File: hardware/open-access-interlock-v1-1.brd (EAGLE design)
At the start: 78.7 x 88.9 mm, 23 parts, among them T1 TIP31

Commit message: Ripping up terminal blocks
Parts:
- removed RELAY: (no value), SparkFun-Connectors:SCREWTERMINAL-3.5MM-3
- added JP1: (no value), SparkFun-Connectors:SCREWTERMINAL-3.5MM-4
- ARDUINO: value ARDUINO_SHIELDNO_SILK -> (none)
- R4: value 650ohm -> 650
- moved T1 44.4 mm to (22.9, 17.8), turned to 180 degrees
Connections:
- removed net N$13: RELAY.2, T1.2
- removed net N$23: ARDUINO.A4, R6.P$1
- removed net N$24: ARDUINO.A5, R7.P$1
- new net RELAY_SIGNAL: JP1.1, T1.2
- net N$14: now also ARDUINO.A4
- net N$15: now also ARDUINO.A5
- net V+: now also JP1.2, JP1.3; no longer RELAY.1
- net V-: now also JP1.4
- net VCC: now also R6.P$1, R7.P$1
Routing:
- net N$23: track 31.1 -> 0.00 mm
- net VCC: track 214.7 -> 189.1 mm
- net RELAY_SIGNAL: track 0.00 -> 23.9 mm
- net N$13: track 15.2 -> 0.00 mm
- net N$14: track 6.61 -> 0.00 mm
- net N$24: track 5.61 -> 0.00 mm
- net N$21: track 8.15 -> 13.5 mm
- net N$15: track 4.48 -> 0.00 mm
- net V-: track 0.00 -> 4.02 mm
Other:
- board text added: "0-24V"
- board text added: "V+"
- board text added: "V-"
- board text removed: "COIL"
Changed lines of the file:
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@@
 <setting verticaltext="up"/>
 </settings>
-<grid distance="50" unitdist="mil" unit="mil" style="dots" multiple="1" display="yes" altdistance="1" altunitdist="mm" altunit="mm"/>
+<grid distance="100" unitdist="mil" unit="mil" style="dots" multiple="1" display="yes" altdistance="1" altunitdist="mm" altunit="mm"/>
 <layers>
 <layer number="1" name="Top" color="4" fill="1" visible="yes" active="yes"/>
@@
 <text x="36.83" y="45.72" size="1.016" layer="25" rot="R90" align="top-left">15</text>
 <text x="36.83" y="48.26" size="1.016" layer="25" rot="R90" align="top-left">16</text>
-<text x="8.89" y="10.16" size="1.016" layer="25" rot="R90" align="top-center">GND</text>
-<text x="8.89" y="13.97" size="1.016" layer="25" rot="R90" align="top-center">COIL</text>
-<text x="8.89" y="17.78" size="1.016" layer="25" rot="R90" align="top-center">+5V</text>
+<text x="8.89" y="21.59" size="1.016" layer="25" align="center-left">GND</text>
+<text x="8.89" y="13.97" size="1.016" layer="25" align="center-left">V-</text>
+<text x="8.89" y="17.78" size="1.016" layer="25" align="center-left">V+</text>
 <text x="8.89" y="69.85" size="1.016" layer="25" rot="R90" align="top-center">+5V</text>
 <text x="8.89" y="66.04" size="1.016" layer="25" rot="R90" align="top-center">GND</text>
@@
 <text x="46.99" y="73.66" size="1.016" layer="25" align="center-right">9</text>
 <text x="46.99" y="55.88" size="1.016" layer="25" align="center">16</text>
+<text x="8.89" y="24.765" size="1.016" layer="25" align="center-left">0-24V</text>
 </plain>
 <attributes>
@@
 </autorouter>
 <elements>
-<element name="ARDUINO" library="SparkFun" package="DUEMILANOVE_VIAS" value="ARDUINO_SHIELDNO_SILK" x="11.43" y="25.4"/>
+<element name="ARDUINO" library="SparkFun" package="DUEMILANOVE_VIAS" value="" x="11.43" y="25.4"/>
 <element name="RELAY_LED" library="led" package="LED5MM" value="GRN" x="73.66" y="12.7" smashed="yes" rot="R90">
 <attribute name="NAME" x="71.8566" y="-0.635" size="1.27" layer="25" ratio="10" rot="R90"/>
@@
 <element name="LCD" library="adafruit" package="LCD1602" value="HD44780LCD-1602" x="68.58" y="2.54" smashed="yes" rot="R90"/>
 <element name="SPKR" library="adafruit" package="PS12" value="SPEAKER/PS12" x="6.35" y="48.26" rot="R180"/>
-<element name="R4" library="SparkFun" package="AXIAL-0.3" value="650ohm" x="24.13" y="35.56" smashed="yes" rot="R180">
+<element name="R4" library="SparkFun" package="AXIAL-0.3" value="650" x="24.13" y="35.56" smashed="yes" rot="R180">
 <attribute name="NAME" x="26.67" y="34.29" size="0.8128" layer="25" font="vector" rot="R180"/>
 <attribute name="VALUE" x="26.162" y="35.941" size="1.016" layer="21" font="vector" ratio="15" rot="R180"/>
@@
 <attribute name="VALUE" x="66.929" y="64.262" size="1.016" layer="21" font="vector" ratio="15" rot="R270"/>
 </element>
-<element name="RELAY" library="SparkFun-Connectors" package="SCREWTERMINAL-3.5MM-3" value="" x="5.08" y="17.78" smashed="yes" rot="R270">
-<attribute name="NAME" x="8.89" y="21.59" size="1.016" layer="25" rot="R180"/>
-<attribute name="VALUE" x="6.35" y="19.05" size="0.4064" layer="27" rot="R270"/>
-</element>
 <element name="READER" library="SparkFun-Connectors" package="SCREWTERMINAL-3.5MM-4" value="" x="5.08" y="69.85" smashed="yes" rot="R270">
 <attribute name="NAME" x="5.08" y="72.39" size="1.016" layer="25"/>
 <attribute name="VALUE" x="6.35" y="71.12" size="0.4064" layer="27" rot="R270"/>
 </element>
-<element name="T1" library="transistor" package="TO220" value="TIP31" x="-17.78" y="0"/>
+<element name="T1" library="transistor" package="TO220" value="TIP31" x="22.86" y="17.78" rot="R180"/>
+<element name="JP1" library="SparkFun-Connectors" package="SCREWTERMINAL-3.5MM-4" value="" x="-5.08" y="-12.7"/>
 </elements>
 <signals>
@@
 <wire x1="13.97" y1="82.55" x2="5.08" y2="73.66" width="0.4064" layer="1"/>
 <contactref element="READER" pad="1"/>
-<wire x1="35.12" y1="13.08" x2="16.13" y2="13.08" width="0.4064" layer="16"/>
-<wire x1="16.13" y1="13.08" x2="11.43" y2="17.78" width="0.4064" layer="16"/>
 <wire x1="5.08" y1="73.66" x2="5.08" y2="69.85" width="0.4064" layer="1"/>
 <wire x1="20.685" y1="74.66" x2="20.685" y2="74.025" width="0.4064" layer="1"/>
@@
 <wire x1="10.16" y1="71.12" x2="8.89" y2="69.85" width="0.4064" layer="1"/>
 <wire x1="8.89" y1="69.85" x2="5.08" y2="69.85" width="0.4064" layer="1"/>
+<contactref element="R6" pad="P$1"/>
+<contactref element="R7" pad="P$1"/>
+<wire x1="48.26" y1="68.58" x2="67.31" y2="66.04" width="0" layer="19" extent="1-1"/>
+<wire x1="71.12" y1="38.1" x2="62.23" y2="41.91" width="0" layer="19" extent="1-1"/>
 </signal>
 <signal name="N$5">
@@
 <contactref element="SHIFT" pad="13"/>
 <contactref element="EXTEND" pad="2"/>
-<contactref element="LOGOUT" pad="2"/>
 <contactref element="ARDUINO" pad="GND@0"/>
-<contactref element="R3" pad="P$1"/>
 <contactref element="SPKR" pad="P$2"/>
 <contactref element="R2" pad="P$1"/>
@@
 <contactref element="READER" pad="2"/>
 <contactref element="R5" pad="P$2"/>
+<contactref element="LOGOUT" pad="2"/>
+<contactref element="R3" pad="P$1"/>
 </signal>
 <signal name="N$3">
@@
 <via x="53.34" y="45.72" extent="1-16" drill="0.3048"/>
 </signal>
-<signal name="N$13">
-<contactref element="RELAY" pad="2"/>
-<wire x1="19.05" y1="16.51" x2="16.51" y2="13.97" width="0.4064" layer="1"/>
-<wire x1="16.51" y1="13.97" x2="5.39" y2="13.97" width="0.4064" layer="1"/>
-<wire x1="5.39" y1="13.97" x2="5.08" y2="14.28" width="0.4064" layer="1"/>
-<contactref element="T1" pad="2"/>
-<wire x1="5.08" y1="14.28" x2="-17.78" y2="-6.35" width="0" layer="19" extent="1-1"/>
-</signal>
 <signal name="N$16">
 <contactref element="RELAY_LED" pad="K"/>
@@
 <contactref element="R5" pad="P$1"/>
 <wire x1="20.32" y1="35.56" x2="20.32" y2="30.48" width="0.4064" layer="1"/>
-<wire x1="20.32" y1="30.48" x2="20.32" y2="29.21" width="0.4064" layer="1"/>
-<wire x1="20.32" y1="29.21" x2="21.59" y2="27.94" width="0.4064" layer="1"/>
 <contactref element="T1" pad="1"/>
-<wire x1="-20.32" y1="-6.35" x2="20.32" y2="29.21" width="0" layer="19" extent="1-1"/>
-</signal>
-<signal name="N$14">
-<contactref element="LOGOUT" pad="4"/>
-<contactref element="R6" pad="P$2"/>
-<wire x1="75.9206" y1="26.1112" x2="75.4888" y2="26.1112" width="0.4064" layer="1"/>
-<wire x1="75.4888" y1="26.1112" x2="71.12" y2="30.48" width="0.4064" layer="1"/>
-</signal>
-<signal name="N$15">
-<contactref element="EXTEND" pad="4"/>
-<contactref element="R7" pad="P$2"/>
-<wire x1="71.3994" y1="58.9788" x2="71.3994" y2="58.6994" width="0.4064" layer="1"/>
-<wire x1="71.3994" y1="58.6994" x2="71.12" y2="58.42" width="0.4064" layer="1"/>
-<wire x1="71.12" y1="58.42" x2="67.31" y2="58.42" width="0.4064" layer="1"/>
-</signal>
-<signal name="N$23">
-<contactref element="R6" pad="P$1"/>
-<contactref element="ARDUINO" pad="A4"/>
-<wire x1="71.12" y1="38.1" x2="71.12" y2="49.53" width="0.4064" layer="1"/>
-<wire x1="71.12" y1="49.53" x2="64.77" y2="55.88" width="0.4064" layer="1"/>
-<wire x1="64.77" y1="55.88" x2="64.77" y2="63.5" width="0.4064" layer="1"/>
-<wire x1="64.77" y1="63.5" x2="63.5" y2="64.77" width="0.4064" layer="1"/>
-<wire x1="63.5" y1="64.77" x2="62.23" y2="64.77" width="0.4064" layer="1"/>
-</signal>
-<signal name="N$24">
-<contactref element="R7" pad="P$1"/>
-<contactref element="ARDUINO" pad="A5"/>
-<wire x1="67.31" y1="66.04" x2="66.04" y2="67.31" width="0.4064" layer="1"/>
-<wire x1="66.04" y1="67.31" x2="62.23" y2="67.31" width="0.4064" layer="1"/>
-</signal>
-<signal name="V+">
-<contactref element="RELAY" pad="1"/>
+<wire x1="20.32" y1="30.48" x2="25.4" y2="25.4" width="0.4064" layer="1"/>
+<wire x1="25.4" y1="25.4" x2="25.4" y2="24.13" width="0.4064" layer="1"/>
 </signal>
 <signal name="V-">
 <contactref element="T1" pad="3"/>
+<wire x1="17.4804" y1="21.2904" x2="20.32" y2="24.13" width="1.4224" layer="1"/>
+<contactref element="JP1" pad="4"/>
+<wire x1="5.42" y1="-12.7" x2="17.4804" y2="21.2904" width="0" layer="19" extent="1-1"/>
+</signal>
+<signal name="N$14">
+<contactref element="ARDUINO" pad="A4"/>
+<contactref element="R6" pad="P$2"/>
+<contactref element="LOGOUT" pad="4"/>
+<wire x1="71.12" y1="30.48" x2="62.23" y2="64.77" width="0" layer="19" extent="1-1"/>
+<wire x1="75.9206" y1="26.1112" x2="71.12" y2="30.48" width="0" layer="19" extent="1-1"/>
+</signal>
+<signal name="N$15">
+<contactref element="ARDUINO" pad="A5"/>
+<contactref element="R7" pad="P$2"/>
+<contactref element="EXTEND" pad="4"/>
+<wire x1="67.31" y1="58.42" x2="71.3994" y2="58.9788" width="0" layer="19" extent="1-1"/>
+<wire x1="62.23" y1="67.31" x2="67.31" y2="58.42" width="0" layer="19" extent="1-1"/>
+</signal>
+<signal name="V+">
+<contactref element="JP1" pad="3"/>
+<contactref element="JP1" pad="2"/>
+<wire x1="-1.58" y1="-12.7" x2="1.92" y2="-12.7" width="0" layer="19" extent="1-1"/>
+</signal>
+<signal name="RELAY_SIGNAL">
+<contactref element="JP1" pad="1"/>
+<contactref element="T1" pad="2"/>
+<wire x1="5.39" y1="13.97" x2="16.51" y2="13.97" width="1.4224" layer="1"/>
+<wire x1="16.51" y1="13.97" x2="22.86" y2="20.32" width="1.4224" layer="1"/>
+<wire x1="22.86" y1="20.32" x2="22.86" y2="24.13" width="1.4224" layer="1"/>
+<wire x1="5.39" y1="13.97" x2="-5.08" y2="-12.7" width="0" layer="19" extent="1-1"/>
 </signal>
 </signals>

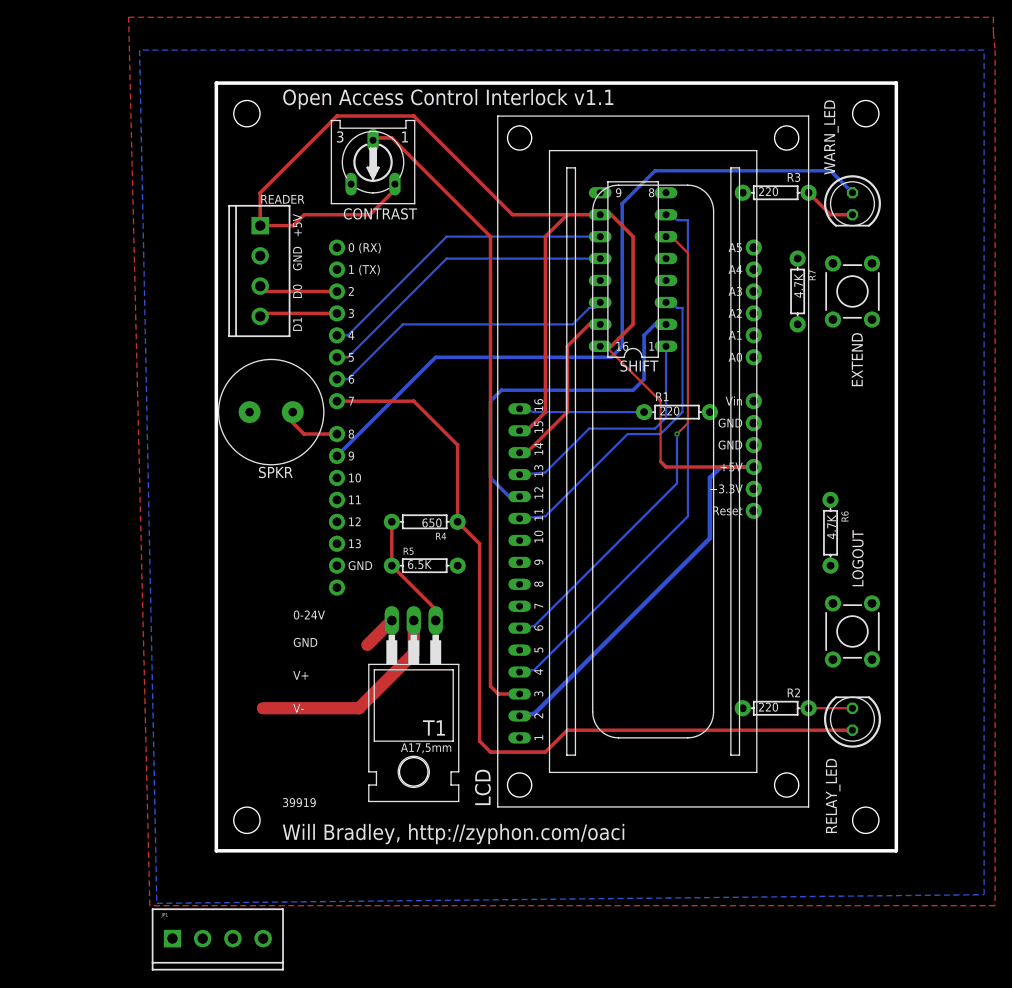
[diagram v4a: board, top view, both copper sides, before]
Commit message: Mounting holes, routing tweaks
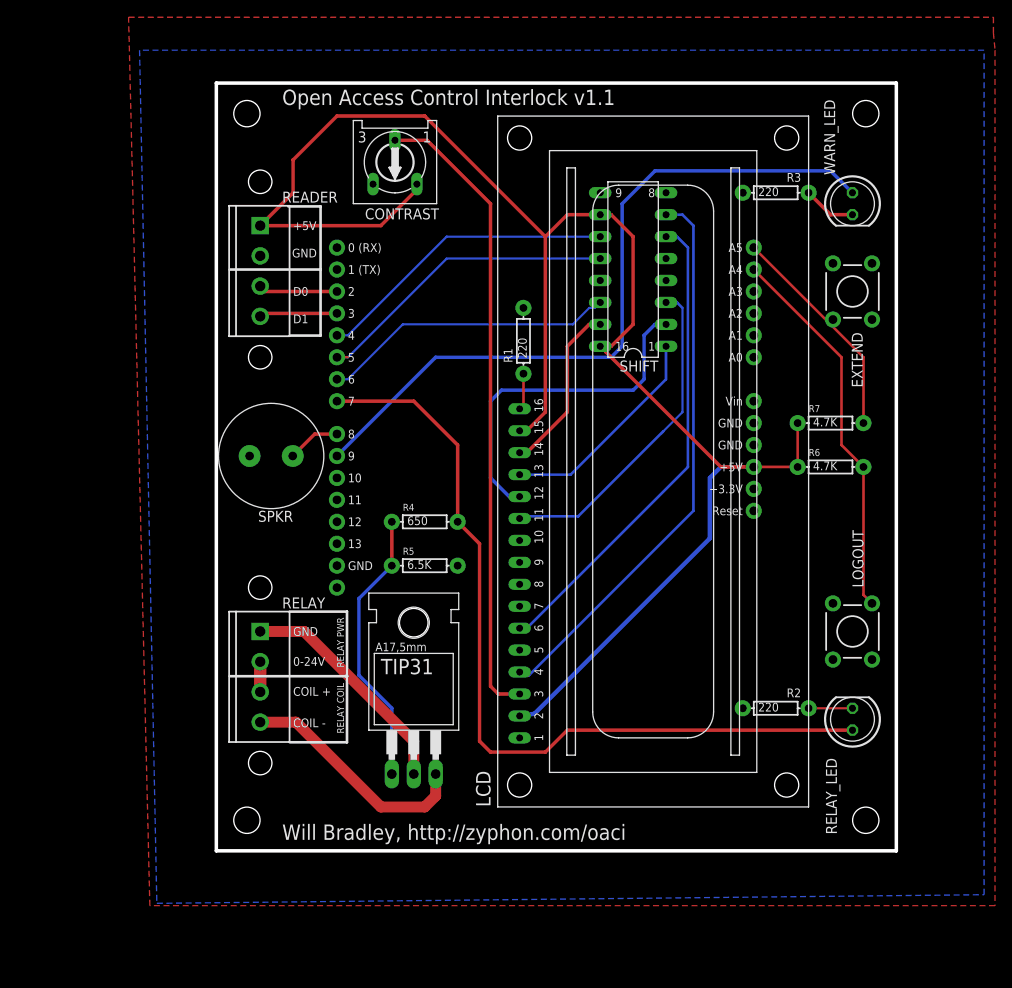
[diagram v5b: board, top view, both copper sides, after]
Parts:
- removed JP1: (no value), SparkFun-Connectors:SCREWTERMINAL-3.5MM-4
- removed T1: TIP31, transistor:TO220
- added RELAY: (no value), SparkFun-Connectors:SCREWTERMINAL-3.5MM-4
- added TIP31: TIP31, transistor:TO220
- SPKR: value SPEAKER/PS12 -> (none)
- moved R1 19.6 mm to (35.6, 56.5), turned to 90 degrees
- moved R7 15.7 mm to (71.1, 47.0), turned to 0 degrees
- moved R6 7.62 mm to (71.1, 41.9), turned to 0 degrees
- moved SPKR 5.08 mm to (6.35, 43.2)
- moved CONTRAST 2.54 mm to (20.7, 77.2)
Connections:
- net GND: now also ARDUINO.GND@1, ARDUINO.GND@2
- net N$21: now also TIP31.1; no longer T1.1
- net RELAY_SIGNAL: now also RELAY.1, TIP31.2; no longer JP1.1, T1.2
- net V+: now also RELAY.2, RELAY.3; no longer JP1.2, JP1.3
- net V-: now also RELAY.4, TIP31.3; no longer JP1.4, T1.3
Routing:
- net N$14: track 0.00 -> 44.3 mm
- net N$15: track 0.00 -> 26.4 mm
- net V-: track 4.02 -> 27.5 mm
- net N$21: track 13.5 -> 32.4 mm
- net N$19: track 14.5 -> 4.25 mm
- net VCC: track 189.1 -> 195.9 mm
- net V+: track 0.00 -> 3.50 mm
- net RELAY_SIGNAL: track 23.9 -> 26.9 mm
- net N$3: track 27.8 -> 25.3 mm
- net N$11: track 55.6 -> 56.6 mm, vias 1 -> 0
- net N$17: track 64.0 -> 64.9 mm
- net N$10: track 6.89 -> 6.17 mm
- net N$12: track 38.1 -> 38.6 mm
- net N$18: track 74.3 -> 73.7 mm
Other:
- board text added: "COIL +"
- board text added: "COIL -"
- board text added: "RELAY COIL"
- board text added: "RELAY PWR"
- board text removed: "39919"
- board text removed: "V+"
- board text removed: "V-"
